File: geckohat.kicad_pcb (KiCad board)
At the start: 2 copper layers, 65 x 56 mm, 63 parts, among them J1 CONN_02X20, J2 TEST_1P, U1 EFM32JG1B100F128GM32, U2 LP2985LV, U3 CAT24C32, Y1 38.4 MHz, Y2 32kHz

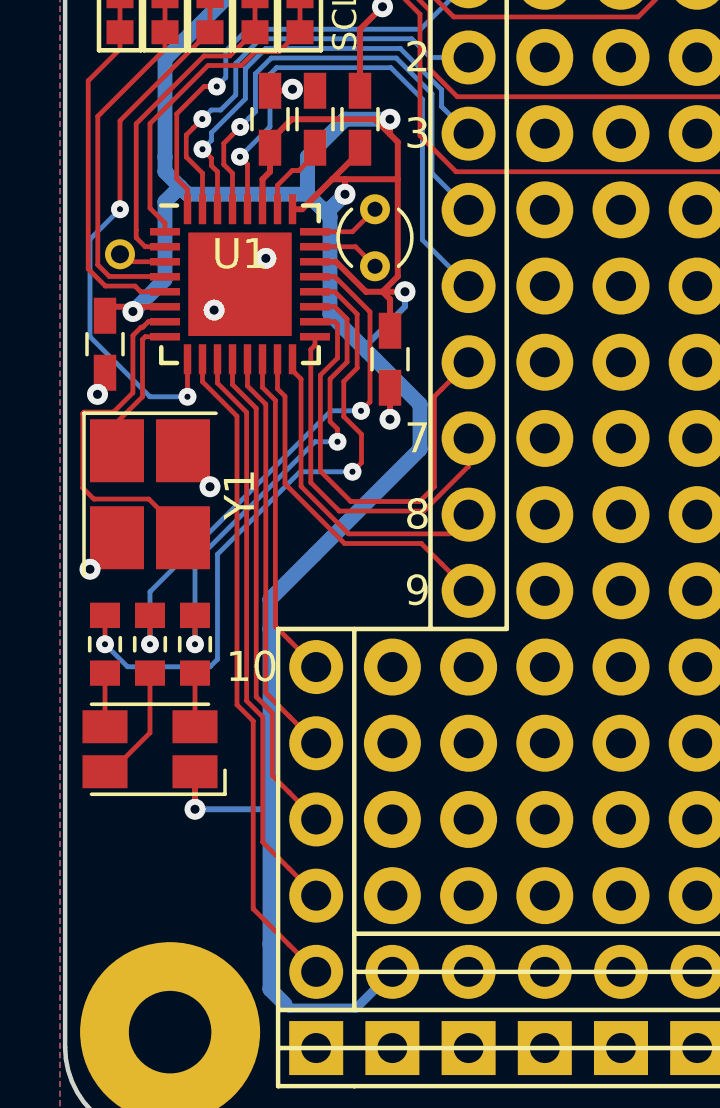
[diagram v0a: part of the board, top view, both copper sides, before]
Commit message: Silkscreen updates
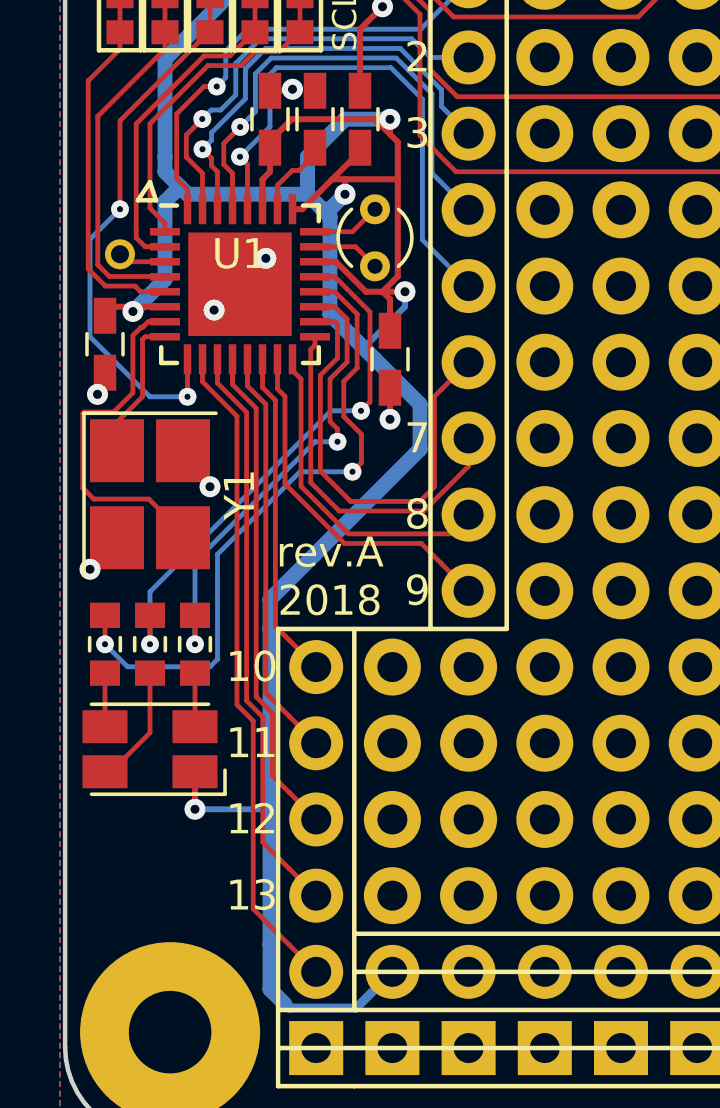
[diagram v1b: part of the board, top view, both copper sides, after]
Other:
- board text added: "11"
- board text added: "12"
- board text added: "13"
- board text added: "Gecko pi hat"
- board text added: "rev.A 2018"
- board text removed: "Gecko RPi hat"
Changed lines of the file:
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@@
     (area 121.094999 71.354999 186.245001 127.505001)
     (thickness 1.6)
-    (drawings 31)
+    (drawings 38)
     (tracks 705)
     (zones 0)
@@
     (37 F.SilkS user)
     (38 B.Mask user hide)
-    (39 F.Mask user hide)
+    (39 F.Mask user)
     (40 Dwgs.User user hide)
     (41 Cmts.User user)
@@
     (zone_45_only no)
     (trace_min 0.16)
-    (segment_width 0.2)
+    (segment_width 0.15)
     (edge_width 0.15)
     (via_size 0.6)
@@
     )
   )
+  (gr_text 11 (at 128.27 114.3) (layer F.SilkS)
+    (effects (font (size 1 1) (thickness 0.2)) (justify right))
+  )
+  (gr_text 13 (at 128.27 119.38) (layer F.SilkS)
+    (effects (font (size 1 1) (thickness 0.2)) (justify right))
+  )
+  (gr_text 12 (at 128.27 116.84) (layer F.SilkS)
+    (effects (font (size 1 1) (thickness 0.2)) (justify right))
+  )
+  (gr_text "rev.A\n2018" (at 130 108.75) (layer F.SilkS)
+    (effects (font (size 1 1) (thickness 0.2)))
+  )
+  (gr_line (start 123.6 96.2) (end 124 95.6) (layer F.SilkS) (width 0.15))
+  (gr_line (start 124.2 96.2) (end 123.6 96.2) (layer F.SilkS) (width 0.15))
+  (gr_line (start 124.2 96.2) (end 124 95.6) (layer F.SilkS) (width 0.15))
   (gr_text 3.3V (at 125.5 80.75) (layer B.SilkS)
     (effects (font (size 1 1) (thickness 0.2)) (justify mirror))
@@
     (effects (font (size 1 1) (thickness 0.25)))
   )
-  (gr_text "Gecko\nRPi hat" (at 124.25 118.75) (layer F.Mask)
+  (gr_text "Gecko\npi hat" (at 123.75 118.75) (layer F.Mask)
     (effects (font (size 1 1) (thickness 0.25)))
   )

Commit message: Specify part numbers
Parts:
- D1: value LED_ARGB -> ASMB-MTB0-0A3A2
- U2: value LP2985LV -> AP2210K-3.3
- Y1: value 38.4 MHz -> TSX-3225 38.4000MF10Z-AS3
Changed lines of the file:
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@@
     (links 194)
     (no_connects 18)
-    (area 121.094999 71.354999 186.245001 127.505001)
+    (area 116.411429 69.265 187.000001 129.465)
     (thickness 1.6)
     (drawings 38)
@@
     (zone_45_only no)
     (trace_min 0.16)
-    (segment_width 0.15)
+    (segment_width 0.2)
     (edge_width 0.15)
     (via_size 0.6)
@@
       (effects (font (size 1 1) (thickness 0.15)))
     )
-    (fp_text value LP2985LV (at 0 2.9 270) (layer F.Fab)
+    (fp_text value AP2210K-3.3 (at 0 2.9 270) (layer F.Fab)
       (effects (font (size 1 1) (thickness 0.15)))
     )
@@
       (effects (font (size 1 1) (thickness 0.15)))
     )
-    (fp_text value "38.4 MHz" (at 0 3 270) (layer F.Fab)
+    (fp_text value "TSX-3225 38.4000MF10Z-AS3" (at 0 3 270) (layer F.Fab)
       (effects (font (size 1 1) (thickness 0.15)))
     )
@@
       (effects (font (size 1 1) (thickness 0.15)))
     )
-    (fp_text value LED_ARGB (at 0 2.65 180) (layer F.Fab)
-      (effects (font (size 1 1) (thickness 0.15)))
-    )
+    (fp_text value ASMB-MTB0-0A3A2 (at 0 2.65 180) (layer F.Fab)
+      (effects (font (size 1 1) (thickness 0.15)))
+    )

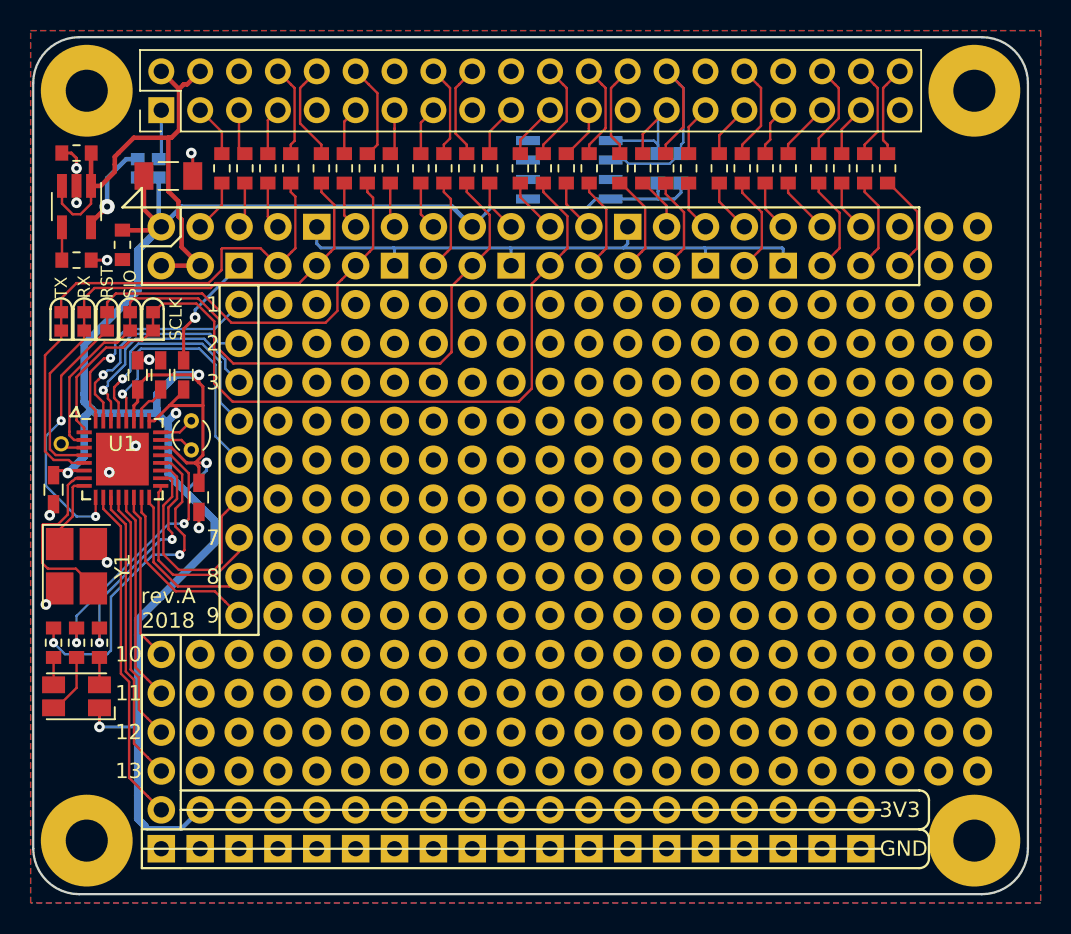
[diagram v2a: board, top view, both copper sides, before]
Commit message: Fix pinout on proto area
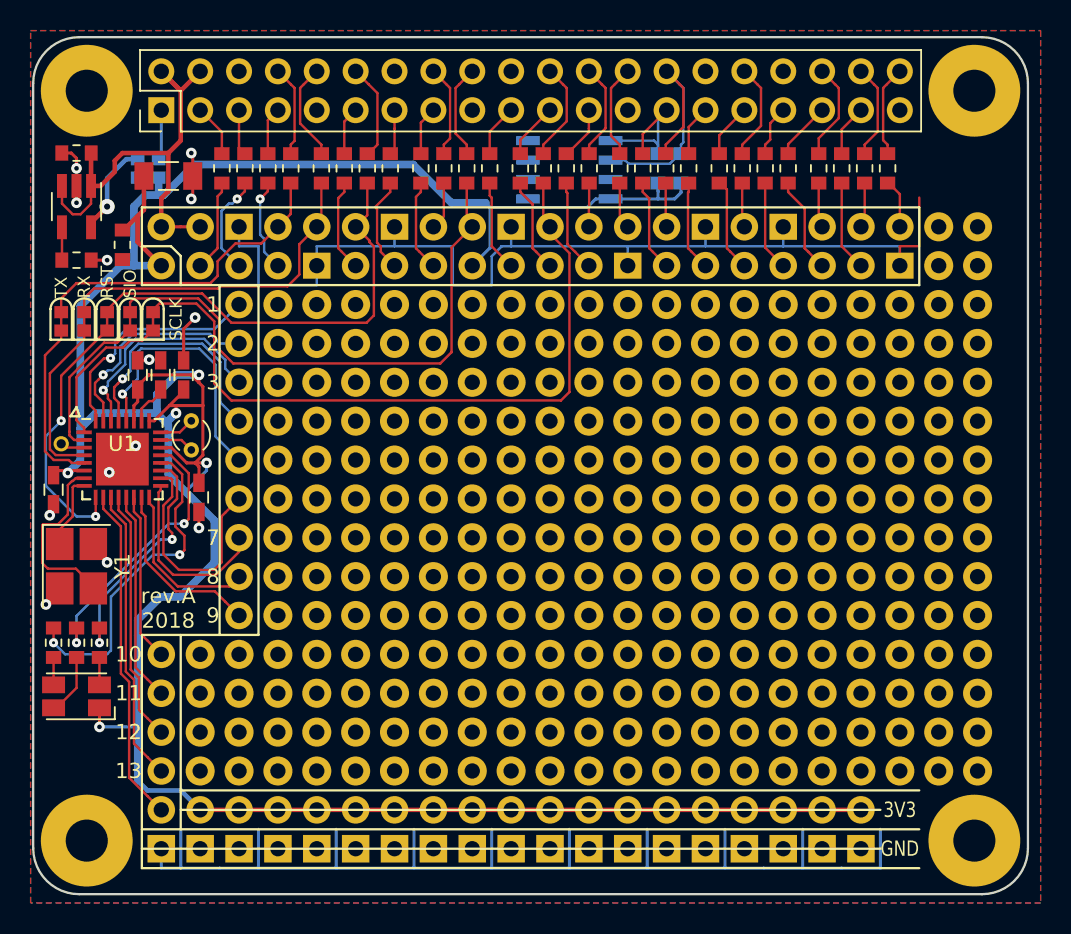
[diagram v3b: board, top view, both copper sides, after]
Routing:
- net GND: track 58.2 -> 159.0 mm, vias 12 -> 13
- net VDD: track 145.4 -> 196.7 mm
- net /PGPIO3: track 3.01 -> 6.66 mm, vias 0 -> 1
- net /PGPIO16: track 6.43 -> 2.95 mm
- net /PGPIO12: track 6.40 -> 2.92 mm
- net /PGPIO21: track 6.72 -> 3.23 mm
- net /PGPIO7: track 6.60 -> 3.15 mm
- net /PID_SC: track 6.37 -> 2.93 mm
- net /PGPIO27: track 2.97 -> 6.33 mm
- net /PGPIO4: track 3.13 -> 6.09 mm, vias 0 -> 1
- net /PGPIO14: track 23.5 -> 20.6 mm
- net /PGPIO23: track 6.06 -> 3.17 mm
- net /PGPIO20: track 6.24 -> 3.36 mm
- net /PGPIO22: track 3.23 -> 6.00 mm
- net /PGPIO17: track 3.36 -> 6.04 mm
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
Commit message: Silk work
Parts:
- C2, C6, C7, C8, C9: footprint Capacitors_SMD:C_0603_HandSoldering -> c_local:C_0603_1608Metric_Pad0.84x1.00mm_HandSolder
- moved D1 1.03 mm to (124.2, 115.5)
- moved R1 1.03 mm to (124.2, 112.0)
- moved R2 1.03 mm to (122.8, 112.0)
- moved R3 1.03 mm to (125.8, 112.0)
- moved Y1 1.03 mm to (124.2, 107.0)
- moved C8 0.50 mm to (122.5, 101.5)
- moved C7 0.25 mm to (132.2, 101.5)
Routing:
- net GND: track 159.0 -> 166.4 mm, vias 13 -> 12
- net VDD: track 196.7 -> 199.5 mm
- net /LED_B: track 18.0 -> 19.1 mm
- net /LED_R: track 15.8 -> 16.9 mm
- net /LED_G: track 22.3 -> 23.3 mm
- net Net-(U1-Pad8): track 4.85 -> 5.75 mm
- net Net-(U1-Pad7): track 11.7 -> 12.4 mm
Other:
- board text added: "elemental.se"
- board text removed: "2018"

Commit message: More silk work
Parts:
- added G***: LOGO, elemental:elemental-25.4mm, B.Cu at (125.5, 94.2)
- added REF***: OSHW-Logo_5.7x6mm_SilkScreen, Symbols:OSHW-Logo_5.7x6mm_SilkScreen, B.Cu at (182.5, 80.8)
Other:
- board text added: "PA0"
- board text added: "PA1"
- board text added: "PC10"
- board text added: "PC11"
- board text added: "PC7"
- board text added: "PC8"
- board text added: "PC9"
- board text added: "PD10"
- board text added: "PD11"
- board text added: "PD12"
- board text added: "PD13"
- board text added: "PD14"
- board text added: "PD15"
- board text added: "PD9"
- board text added: "Raspberry Pi Gecko prototyping hat"

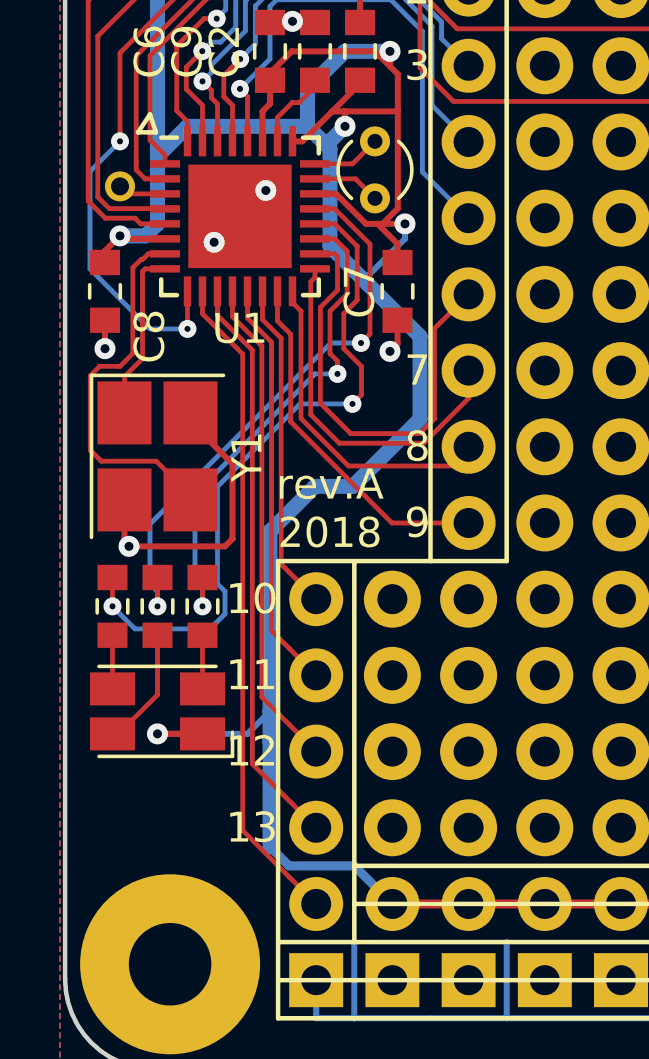
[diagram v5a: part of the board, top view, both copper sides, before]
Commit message: Improve ground fill a bit
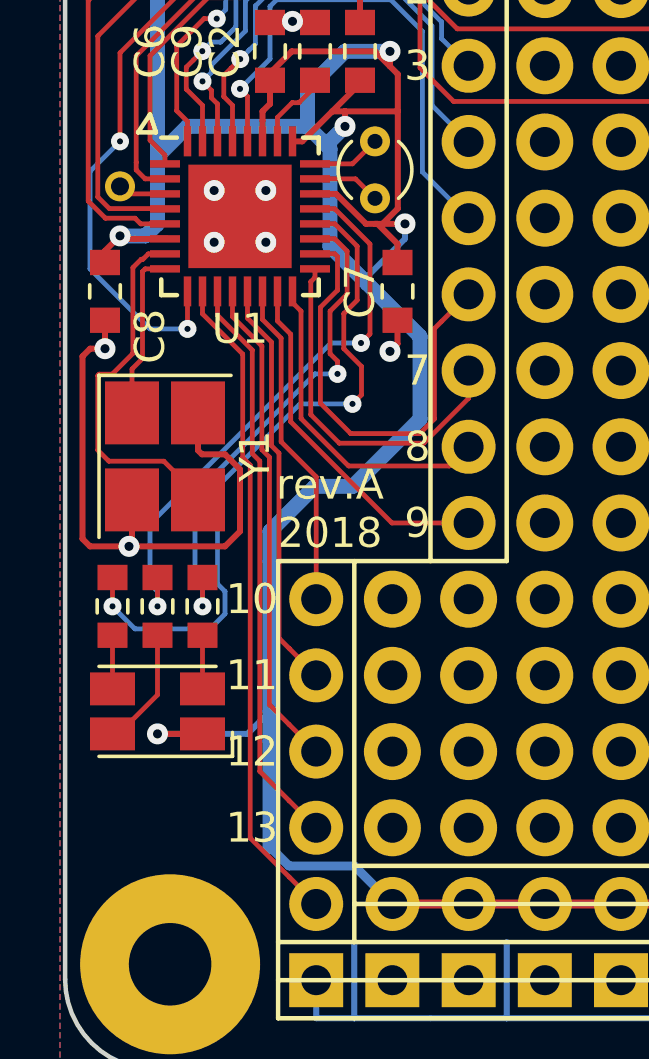
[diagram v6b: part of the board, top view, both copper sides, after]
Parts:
- moved Y1 0.25 mm to (124.5, 107.0)
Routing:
- net GND: track 166.4 -> 179.0 mm, vias 12 -> 14

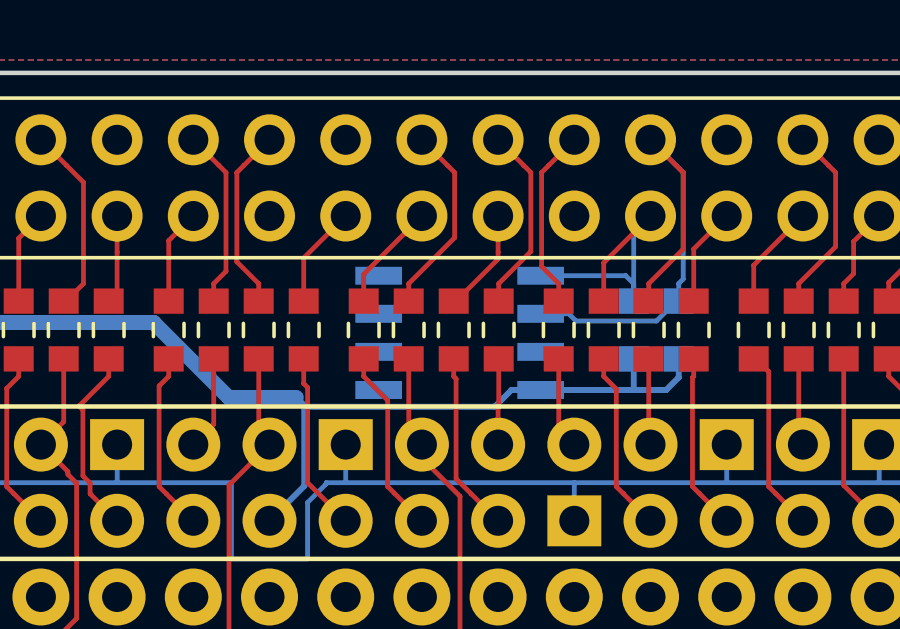
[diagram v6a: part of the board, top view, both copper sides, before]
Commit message: Change to TSSOP EEPROM, so it fits
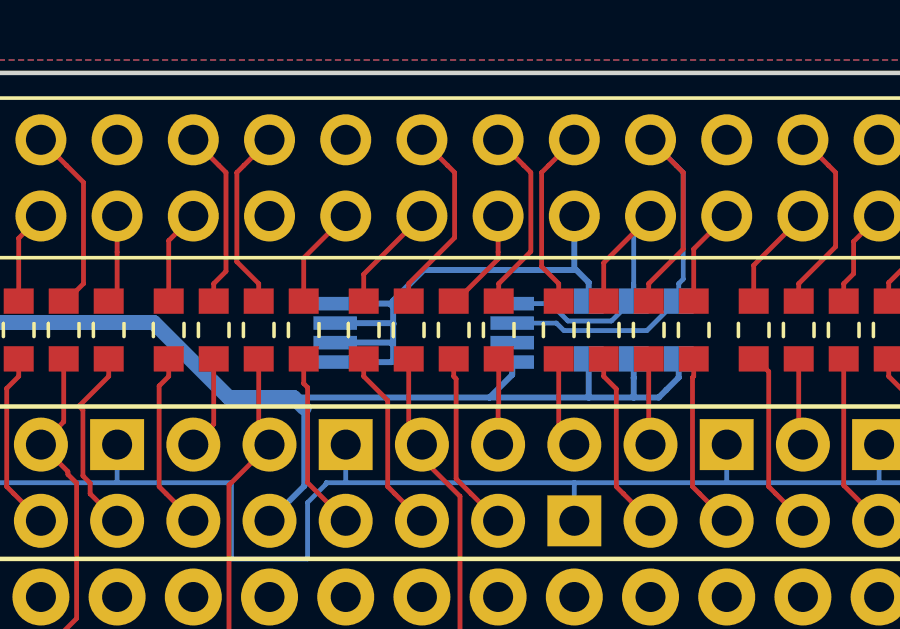
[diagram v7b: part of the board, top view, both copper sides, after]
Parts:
- added C10: 0.1u, c_local:C_0603_1608Metric_Pad0.84x1.00mm_HandSolder, B.Cu at (160.5, 80.0)
- U3: value CAT24C32 -> CAT24C32Y; footprint Housings_SOIC:SOIC-8_3.9x4.9mm_Pitch1.27mm -> Housings_SSOP:TSSOP-8_4.4x3mm_Pitch0.65mm
- moved U3 1.20 mm to (155.0, 80.1)
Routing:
- net GND: track 179.0 -> 199.3 mm
- net VDD: track 199.5 -> 202.7 mm
- net /ID_SD: track 10.3 -> 11.7 mm
- net /ID_SC: track 17.2 -> 18.3 mm

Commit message: Gerber settings
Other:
- rule solder_mask_min_width: 0.35 -> 0.1
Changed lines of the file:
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@@
     (links 196)
     (no_connects 9)
-    (area 121.094999 71.354999 186.245001 127.505001)
+    (area 116.661429 68.79238 187.000001 129.465)
     (thickness 1.6)
     (drawings 59)
@@
     (pad_drill 0.6)
     (pad_to_mask_clearance 0.1)
-    (solder_mask_min_width 0.35)
+    (solder_mask_min_width 0.1)
     (aux_axis_origin 0 0)
-    (visible_elements FFFFEF7F)
+    (visible_elements FFFFFF7F)
     (pcbplotparams
-      (layerselection 0x00030_80000001)
-      (usegerberextensions false)
+      (layerselection 0x010f0_80000001)
+      (usegerberextensions true)
       (excludeedgelayer true)
       (linewidth 0.100000)
@@
       (outputformat 1)
       (mirror false)
-      (drillshape 1)
+      (drillshape 0)
       (scaleselection 1)
-      (outputdirectory ""))
+      (outputdirectory gerber/))
   )
   (net 0 "")
